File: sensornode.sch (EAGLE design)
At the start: 76 parts, among them IC1 CP2104, Q1 mmbt2222, Q2 mmbt2222, Q3 DMG3415U, SW2 KMR2, U1 TSL2591, U2 AP2112-3.3, U3 MCP73831T-2ACI/OT, U4 BMEx80, X2 ESP32_WROOM32_SKINNY, X4 20329

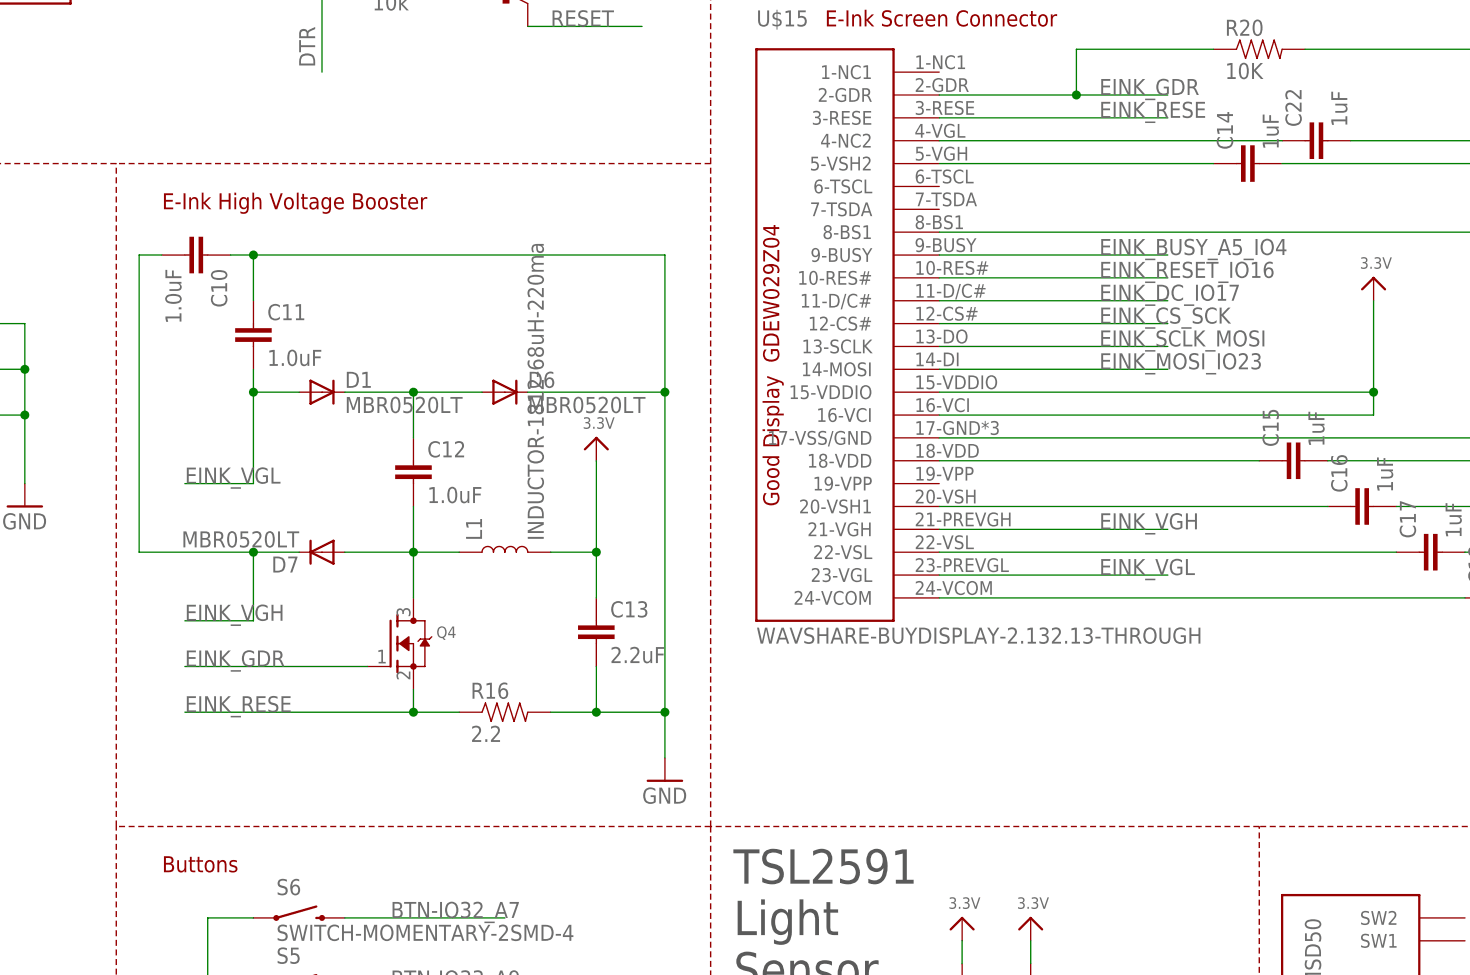
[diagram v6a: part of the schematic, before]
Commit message: Modifications to fix the e-ink screen drivers
So turns out the e-ink screen needs two fixes:
1) The inductor pad is just straight up wrong, so I've replaced that
1.1) I've also moved from a 68uH coil to a 10uH1A coil (matching Good
  Display's DESPI-C02 more closely)
2) The R16 resistor should not, in fact, be 2.2Ohm, it should be 0.47Ohm
	(though I'll note 1Ohm works)

I believe at this point this is now a garaunteed fully working circuit.
Any additional changes would just need to replicate what the DESPI-C02
does, but the original design on the sensornode works with if you swap
the R16 resistor.
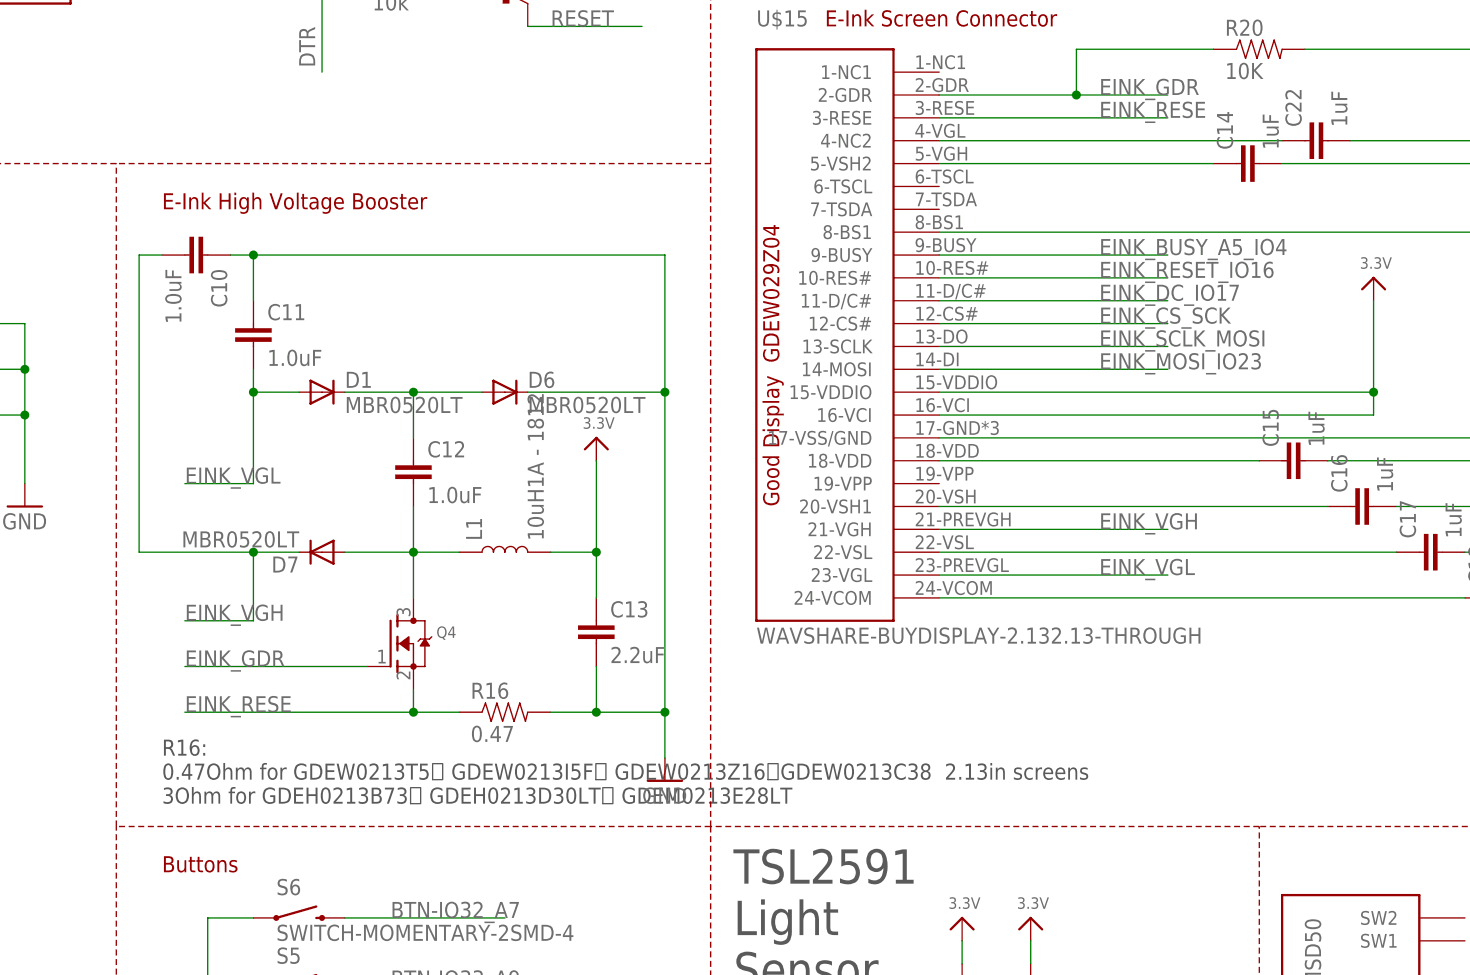
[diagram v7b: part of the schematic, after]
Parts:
- L1: value INDUCTOR-1812-68uH-220ma -> 10uH1A - 1812; device SparkFun-Coils:INDUCTOR-1812 -> John - Inductors:INDUCTOR
- R16: value 2.2 -> 0.47
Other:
- note added: "R16: 0.47Ohm for GDEW0213T5、 GDEW0213I5F、 GDEW0213Z16、GDEW0213C38 2.13in screens 3Ohm for GDEH0213B73、 GDEH0213D30LT、 GDEM0213E28LT"
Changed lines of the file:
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@@
 <part name="C12" library="SparkFun-Capacitors" deviceset="1.0UF" device="-0603-16V-10%" value="1.0uF"/>
 <part name="D7" library="diode" deviceset="MBR0520LT" device=""/>
-<part name="L1" library="SparkFun-Coils" deviceset="INDUCTOR" device="-1812" value="INDUCTOR-1812-68uH-220ma"/>
+<part name="L1" library="John - Inductors" deviceset="INDUCTOR" device="" value="10uH1A - 1812"/>
 <part name="U$2" library="microbuilder" deviceset="3.3V" device=""/>
 <part name="C13" library="SparkFun-Capacitors" deviceset="2.2UF" device="-0603-10V-20%" value="2.2uF"/>
 <part name="Q4" library="adafruit" deviceset="MOSFET-N" device="REFLOW"/>
-<part name="R16" library="SparkFun-Resistors" deviceset="4.7KOHM-1/10W-1%(0603)" device="" value="2.2"/>
+<part name="R16" library="SparkFun-Resistors" deviceset="4.7KOHM-1/10W-1%(0603)" device="" value="0.47"/>
 <part name="U$15" library="Warthog9-Screens" deviceset="WAVSHARE-BUYDISPLAY-2.13" device="2.13-THROUGH" value="WAVSHARE-BUYDISPLAY-2.132.13-THROUGH"/>
 <part name="C14" library="SparkFun-Capacitors" deviceset="0.1UF-25V-5%(0603)" device="" value="1uF"/>
@@
 <wire x1="251.46" y1="71.12" x2="284.48" y2="71.12" width="0.1524" layer="94" style="shortdash"/>
 <wire x1="299.72" y1="22.86" x2="299.72" y2="71.12" width="0.1524" layer="94" style="shortdash"/>
+<text x="76.2" y="53.34" size="1.778" layer="97">R16:
+0.47Ohm for GDEW0213T5、 GDEW0213I5F、 GDEW0213Z16、GDEW0213C38  2.13in screens
+3Ohm for GDEH0213B73、 GDEH0213D30LT、 GDEM0213E28LT </text>
 </plain>
 <instances>
